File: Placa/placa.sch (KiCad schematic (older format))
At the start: 23 parts

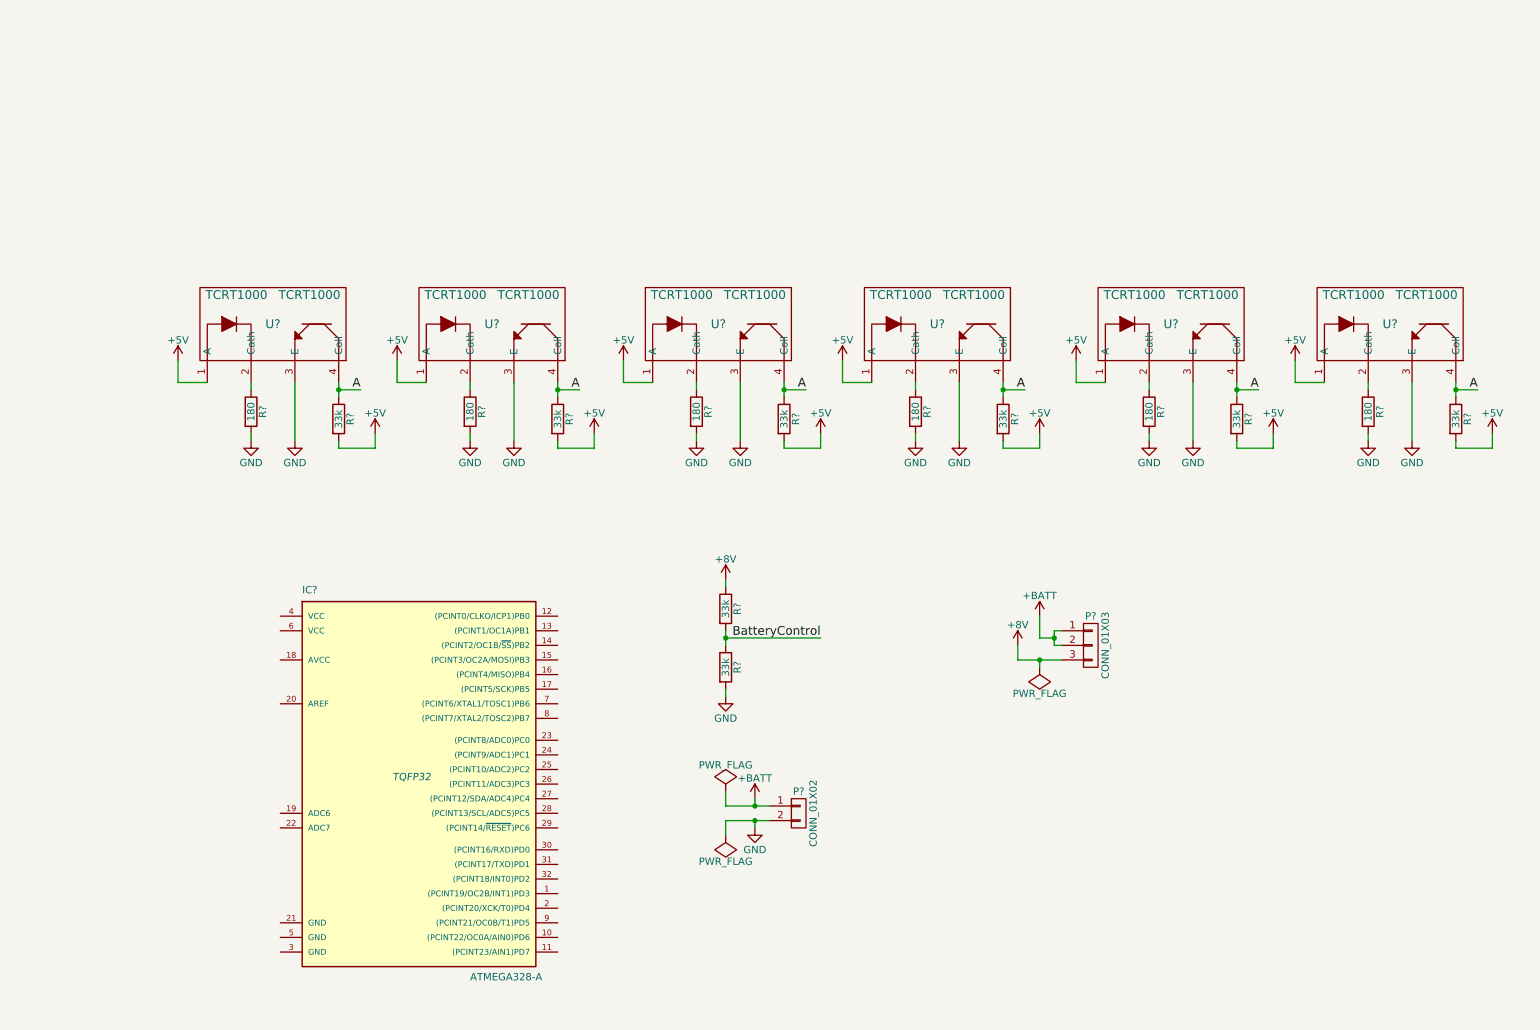
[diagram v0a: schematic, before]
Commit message: Agregados reguladores de tension en el PCB. Falta el puente H
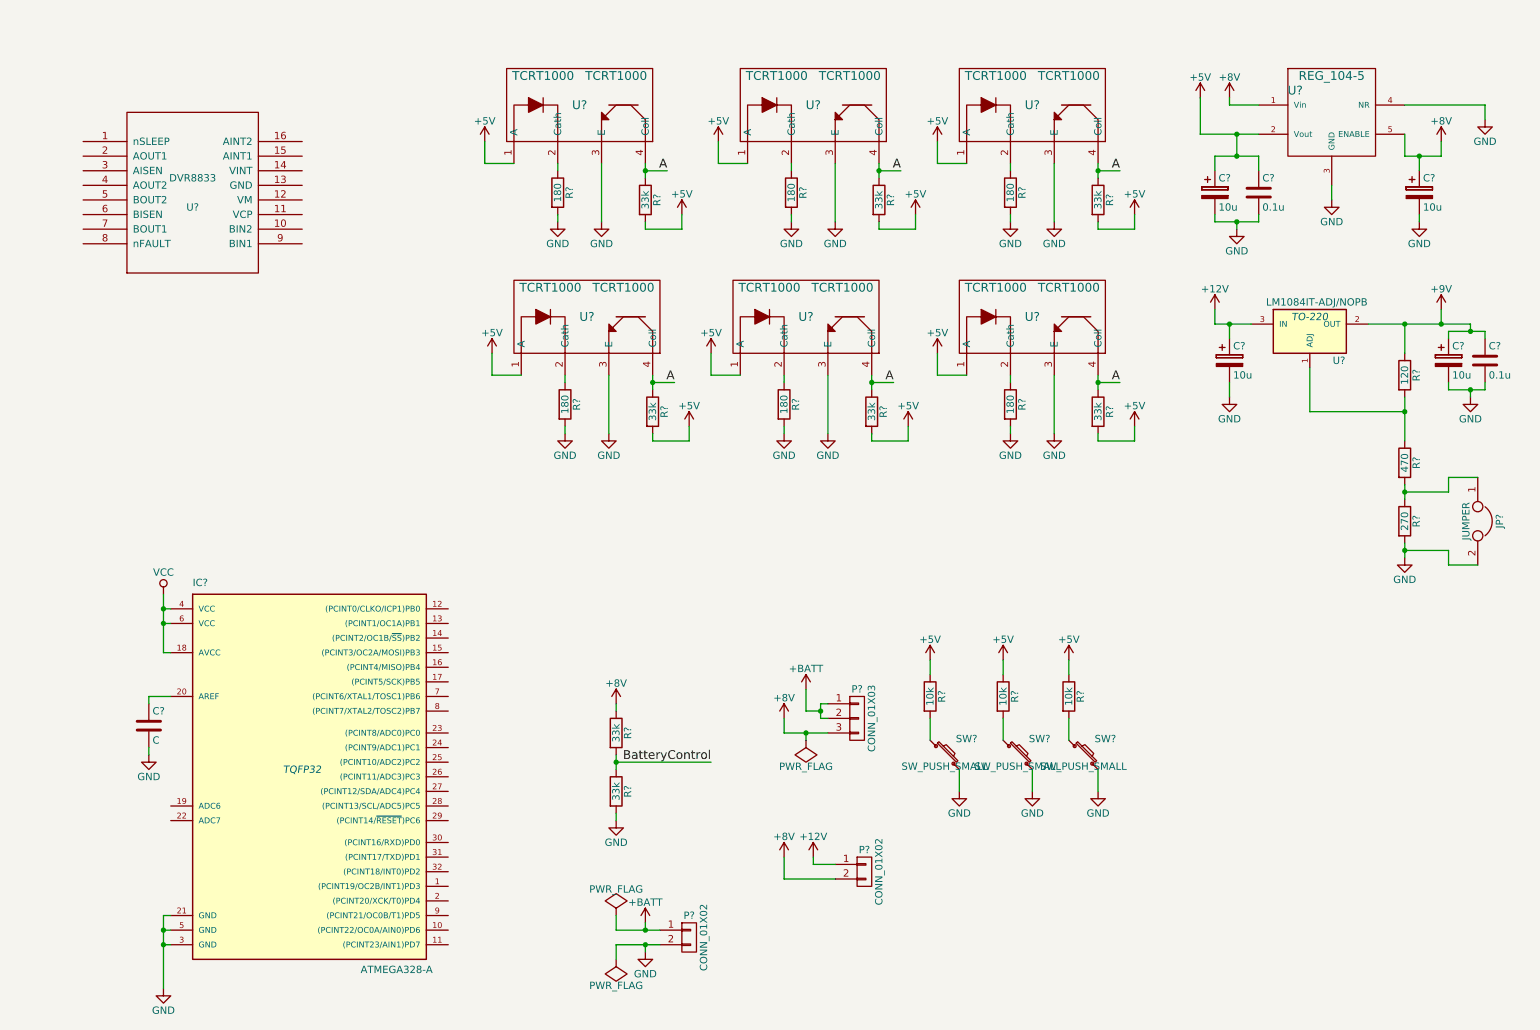
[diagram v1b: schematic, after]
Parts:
- added C? (x4): 10u, symbol CP
- added C? (x2): 0.1u, symbol C
- added C?: C, symbol C
- added JP?: JUMPER, symbol JUMPER
- added P?: CONN_01X02, symbol CONN_01X02
- added R? (x3): 10k, symbol R
- added R?: 120, symbol R
- added R?: 470, symbol R
- added R?: 270, symbol R
- added SW? (x3): SW_PUSH_SMALL, symbol SW_PUSH_SMALL
- added U?: REG_104-5, symbol REG_104-5
- added U?: LM1084IT-ADJ/NOPB, TO-220, symbol LM1084IT-ADJ/NOPB
- added U?: DVR8833, MODULE, symbol DVR8833
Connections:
- net +5V: now also C?.1, C?.1, R?.1, R?.1, R?.1, U?.2 (Vout)
- net +8V: now also C?.1, P?.2 (P2), U?.1 (Vin), U?.5 (ENABLE)
- net GND: now also IC?.21 (GND), IC?.3 (GND), IC?.5 (GND), C?.2, C?.2, C?.2, C?.2, C?.2, C?.2, C?.2, JP?.2, R?.2, SW?.2, SW?.2, SW?.2, U?.3 (GND), U?.4 (NR)
- net VCC: now reaches IC?.18 (AVCC)
- net VCC: now also IC?.4 (VCC), IC?.6 (VCC)
- net at IC?.20 (AREF): now also C?.1
- new net: R?.2, SW?.1 (x3)
- new net: R?.1, R?.2, U?.1 (ADJ)
- new net: JP?.1, R?.1, R?.2
- new net +12V: C?.1, P?.1 (P1), U?.3 (IN)
- new net +9V: C?.1, C?.1, R?.1, U?.2 (OUT)
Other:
- moved on the sheet: IC?, P?, R?, U?

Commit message: Agregados sub-esquemáticos. Avances en la placa.
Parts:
- removed R? (x6): 180, symbol R
- removed R? (x6): 33k, symbol R
- removed U? (x6): TCRT1000, TCRT1000, symbol TCRT1000
- removed U?: DVR8833, MODULE, symbol DVR8833
- added P?: CONN_01X03, symbol CONN_01X03
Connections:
- net labels added: Boton1, Boton2, Boton3, M1IN1, M1IN2, M1OUT1, M1OUT2, M1VCP, M1VINT, M2IN1, M2IN2, M2OUT1, M2OUT2, M2VCP, M2VINT, Sensor1, Sensor2, Sensor3, Sensor4, Sensor5, Sensor6, VDD, VPP
- net labels removed: A, VCC
- wire segments 148 -> 132
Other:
- moved on the sheet: P?, R?, SW?

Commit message: Avances sobre la placa.
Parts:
- removed C? (x4): 10u, symbol CP
- removed C? (x2): 0.1u, symbol C
- removed JP?: JUMPER, symbol JUMPER
- removed P? (x2): CONN_01X03, symbol CONN_01X03
- removed P? (x2): CONN_01X02, symbol CONN_01X02
- removed R?: 120, symbol R
- removed R?: 470, symbol R
- removed R?: 270, symbol R
- removed U?: REG_104-5, symbol REG_104-5
- removed U?: LM1084IT-ADJ/NOPB, TO-220, symbol LM1084IT-ADJ/NOPB
- added D2, D3, D4, D5: LED, LEDs:LED_0805, symbol LED
- added P1: CONN_01X04, Pin_Headers:Pin_Header_Straight_1x04, symbol CONN_01X04
- added P2, P3: CONN_01X02, Pin_Headers:Pin_Header_Straight_1x02, symbol CONN_01X02
- added R2: 10k, Resistors_SMD:R_0805, symbol R
- added R25, R26, R27, R28: 220, Resistors_SMD:R_0805, symbol R
- added SW1: SW_PUSH_SMALL, Buttons_Switches_ThroughHole:SW_PUSH_SMALL, symbol SW_PUSH_SMALL
- C1: renamed from C?; footprint (none) -> Capacitors_ThroughHole:C_Radial_D5_L11_P2
- IC1: renamed from IC?; footprint TQFP32 -> Housings_QFP:TQFP-32_7x7mm_Pitch0.8mm
- R3, R4, R5, R6, R7: renamed from R?; footprint (none) -> Resistors_SMD:R_0805
- SW2, SW3, SW4: renamed from SW?; footprint (none) -> Buttons_Switches_ThroughHole:SW_PUSH_SMALL
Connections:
- net labels added: Habilitador1, Habilitador2, Led1, Led2, Led3, Led4, RX, Reset, TX
- net labels removed: +12V, +9V, M1VCP, M2VCP, VDD
- wire segments 132 -> 106
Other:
- moved on the sheet: R4, R5

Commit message: Más avances en placa. Ignorados archivos bak.
Falta corregir algunas cosas en el esquemático, relacionado con los motores. El pcb está apenas empezado.
Se ignoraron los archivos bak y cache de kicad.
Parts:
- added P12: CONN_02X03, Pin_Headers:Pin_Header_Straight_2x03, symbol CONN_02X03
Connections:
- net labels added: Miso, Mosi, Sck
- wire segments 106 -> 114
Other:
- note added: "Conector Serie"
- note added: "Conector programador ISP\n"
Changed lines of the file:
@@
 LIBS:reg_204-5
 LIBS:DVR8833
-LIBS:placa-cache
 EELAYER 25 0
 EELAYER END
@@
 	10350 5350 10700 5350
 Connection ~ 10700 5350
-Text Label 4100 4950 2    60   ~ 0
+Text Label 4100 4450 2    60   ~ 0
 Boton1
 Text Label 4100 5050 2    60   ~ 0
@@
 F4 "M2VINT" I L 3600 2000 60
 F5 "VM" I L 3600 1050 60
-F7 "M2OUT1" I L 3600 1450 60
-F8 "M2OUT2" I L 3600 1600 60
-F9 "M1IN2" I R 5100 2450 60
-F10 "M1IN1" I R 5100 2250 60
-F11 "M1VINT" I R 5100 2000 60
-F13 "M1OUT1" I R 5100 1450 60
-F14 "M1OUT2" I R 5100 1600 60
+F6 "M2OUT1" I L 3600 1450 60
+F7 "M2OUT2" I L 3600 1600 60
+F8 "M1IN2" I R 5100 2450 60
+F9 "M1IN1" I R 5100 2250 60
+F10 "M1VINT" I R 5100 2000 60
+F11 "M1OUT1" I R 5100 1450 60
+F12 "M1OUT2" I R 5100 1600 60
 $EndSheet
 $Sheet
@@
 Text Label 8200 1900 2    60   ~ 0
 Habilitador2
-Text Label 4300 4850 2    60   ~ 0
+Text Label 4350 6750 2    60   ~ 0
 Habilitador2
-Text Label 4300 4750 2    60   ~ 0
+Text Label 4300 6450 2    60   ~ 0
 Habilitador1
 Wire Wire Line
-	4300 4850 3750 4850
-Wire Wire Line
-	3750 4750 4300 4750
+	3750 4850 4700 4850
+Wire Wire Line
+	3750 4750 4700 4750
 Text Label 8550 4200 0    60   ~ 0
 M2OUT1
 Text Label 8550 4300 0    60   ~ 0
 M2OUT2
-Text Label 4100 6350 2    60   ~ 0
-M2VINT
 Text Label 4050 4550 2    60   ~ 0
 M2IN1
@@
 Text Label 8550 3700 0    60   ~ 0
 M1OUT2
-Text Label 4100 6250 2    60   ~ 0
-M1VINT
 Text Label 4050 6650 2    60   ~ 0
 M1IN1
@@
 	4050 4650 3750 4650
 Wire Wire Line
-	4100 4950 3750 4950
+	3750 4950 4650 4950
 Wire Wire Line
 	4100 5050 3750 5050
@@
 L CONN_01X04 P1
 U 1 1 572D968E
-P 8250 5400
-F 0 "P1" H 8250 5650 50  0000 C CNN
-F 1 "CONN_01X04" V 8350 5400 50  0000 C CNN
-F 2 "Pin_Headers:Pin_Header_Straight_1x04" H 8250 5400 50  0001 C CNN
-F 3 "" H 8250 5400 50  0000 C CNN
-	1    8250 5400
-	1    0    0    -1
-$EndComp
-Wire Wire Line
-	8050 5250 7900 5250
-Wire Wire Line
-	7900 5250 7900 5150
+P 8250 5350
+F 0 "P1" H 8250 5600 50  0000 C CNN
+F 1 "CONN_01X04" V 8350 5350 50  0000 C CNN
+F 2 "Pin_Headers:Pin_Header_Straight_1x04" H 8250 5350 50  0001 C CNN
+F 3 "" H 8250 5350 50  0000 C CNN
+	1    8250 5350
+	1    0    0    -1
+$EndComp
+Wire Wire Line
+	8050 5200 7900 5200
+Wire Wire Line
+	7900 5200 7900 5100
 $Comp
 L +5V #PWR017
 U 1 1 572DB105
-P 7900 5150
-F 0 "#PWR017" H 7900 5000 50  0001 C CNN
-F 1 "+5V" H 7900 5290 50  0000 C CNN
-F 2 "" H 7900 5150 50  0000 C CNN
-F 3 "" H 7900 5150 50  0000 C CNN
-	1    7900 5150
-	1    0    0    -1
-$EndComp
-Wire Wire Line
-	8050 5550 7900 5550
-Text Label 7900 5350 0    60   ~ 0
+P 7900 5100
+F 0 "#PWR017" H 7900 4950 50  0001 C CNN
+F 1 "+5V" H 7900 5240 50  0000 C CNN
+F 2 "" H 7900 5100 50  0000 C CNN
+F 3 "" H 7900 5100 50  0000 C CNN
+	1    7900 5100
+	1    0    0    -1
+$EndComp
+Wire Wire Line
+	8050 5500 7900 5500
+Text Label 7900 5300 0    60   ~ 0
 TX
 Wire Wire Line
-	7600 5450 8050 5450
-Wire Wire Line
-	7900 5350 8050 5350
-Wire Wire Line
-	7600 5450 7600 5550
+	7600 5400 8050 5400
+Wire Wire Line
+	7900 5300 8050 5300
+Wire Wire Line
+	7600 5400 7600 5500
 $Comp
 L GND #PWR018
 U 1 1 572DBC53
-P 7600 5550
-F 0 "#PWR018" H 7600 5300 50  0001 C CNN
-F 1 "GND" H 7600 5400 50  0000 C CNN
-F 2 "" H 7600 5550 50  0000 C CNN
-F 3 "" H 7600 5550 50  0000 C CNN
-	1    7600 5550
-	1    0    0    -1
-$EndComp
-Text Label 7900 5550 0    60   ~ 0
+P 7600 5500
+F 0 "#PWR018" H 7600 5250 50  0001 C CNN
+F 1 "GND" H 7600 5350 50  0000 C CNN
+F 2 "" H 7600 5500 50  0000 C CNN
+F 3 "" H 7600 5500 50  0000 C CNN
+	1    7600 5500
+	1    0    0    -1
+$EndComp
+Text Label 7900 5500 0    60   ~ 0
 RX
 Text Label 3900 6150 2    60   ~ 0
@@
 Text Label 1800 3550 0    60   ~ 0
 Led2
-Text Label 4000 6450 2    60   ~ 0
+Text Label 4000 4750 2    60   ~ 0
 Led1
 Wire Wire Line
-	3750 4450 4000 4450
-Text Label 4000 6750 2    60   ~ 0
-Led2
-Wire Wire Line
-	3750 6450 4000 6450
-Text Label 4000 4450 2    60   ~ 0
+	3750 4450 4100 4450
+Wire Wire Line
+	3750 6450 4300 6450
+Text Label 4000 4950 2    60   ~ 0
 Led3
 Wire Wire Line
-	4000 6750 3750 6750
+	4350 6750 3750 6750
 Text Label 4000 5800 2    60   ~ 0
 Led4
@@
 Wire Wire Line
 	4000 5800 3750 5800
+$Comp
+L CONN_02X03 P12
+U 1 1 57365B2B
+P 6900 3850
+F 0 "P12" H 6900 4050 50  0000 C CNN
+F 1 "CONN_02X03" H 6900 3650 50  0000 C CNN
+F 2 "Pin_Headers:Pin_Header_Straight_2x03" H 6900 2650 50  0001 C CNN
+F 3 "" H 6900 2650 50  0000 C CNN
+	1    6900 3850
+	1    0    0    -1
+$EndComp
+Text Label 6400 3750 0    60   ~ 0
+Miso
+Wire Wire Line
+	6400 3750 6650 3750
+Wire Wire Line
+	7150 3750 7400 3750
+Wire Wire Line
+	7400 3750 7400 3600
+$Comp
+L +5V #PWR025
+U 1 1 573660BC
+P 7400 3600
+F 0 "#PWR025" H 7400 3450 50  0001 C CNN
+F 1 "+5V" H 7400 3740 50  0000 C CNN
+F 2 "" H 7400 3600 50  0000 C CNN
+F 3 "" H 7400 3600 50  0000 C CNN
+	1    7400 3600
+	1    0    0    -1
+$EndComp
+Wire Wire Line
+	7150 3950 7400 3950
+Wire Wire Line
+	7400 3950 7400 4100
+$Comp
+L GND #PWR026
+U 1 1 57366261
+P 7400 4100
+F 0 "#PWR026" H 7400 3850 50  0001 C CNN
+F 1 "GND" H 7400 3950 50  0000 C CNN
+F 2 "" H 7400 4100 50  0000 C CNN
+F 3 "" H 7400 4100 50  0000 C CNN
+	1    7400 4100
+	1    0    0    -1
+$EndComp
+Text Label 7400 3850 2    60   ~ 0
+Mosi
+Wire Wire Line
+	7400 3850 7150 3850
+Text Label 6450 3850 0    60   ~ 0
+Sck
+Wire Wire Line
+	6450 3850 6650 3850
+Text Label 6350 3950 0    60   ~ 0
+Reset
+Wire Wire Line
+	6350 3950 6650 3950
+Text Label 4700 4850 2    60   ~ 0
+Miso
+Text Label 4650 4950 2    60   ~ 0
+Sck
+Text Label 4700 4750 2    60   ~ 0
+Mosi
+Text Notes 6400 3350 0    60   ~ 0
+Conector programador ISP\n
+Text Label 4000 4850 2    60   ~ 0
+Led2
+Text Notes 7600 4850 0    60   ~ 0
+Conector Serie
+Wire Notes Line
+	7400 4700 7400 5750
+Wire Notes Line
+	7400 5750 8500 5750
+Wire Notes Line
+	8500 5750 8500 4700
+Wire Notes Line
+	8500 4700 7400 4700
+Wire Notes Line
+	6250 3150 6250 4350
+Wire Notes Line
+	6250 4350 7650 4350
+Wire Notes Line
+	7650 4350 7650 3150
+Wire Notes Line
+	7650 3150 6250 3150
 $EndSCHEMATC

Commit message: Cambio prematuro de etiquetas para saber qué cosas hay que cambiar.
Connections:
- net labels added: BotonExtra, EncoderM1, EncoderM2, M1IN1(PWM), M2IN1(PWM), Sensor7, XTAL1, XTAL2
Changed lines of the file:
@@
 Text Label 4100 4450 2    60   ~ 0
 Boton1
-Text Label 4100 5050 2    60   ~ 0
+Text Label 4350 6750 2    60   ~ 0
 Boton2
-Text Label 4100 5150 2    60   ~ 0
-Boton3
+Text Label 4500 6150 2    60   ~ 0
+BotonExtra
 Text Label 1200 5800 0    60   ~ 0
 BatteryControl
@@
 Text Label 8200 1900 2    60   ~ 0
 Habilitador2
-Text Label 4350 6750 2    60   ~ 0
+Text Label 5550 6100 2    60   ~ 0
 Habilitador2
 Text Label 4300 6450 2    60   ~ 0
@@
 Text Label 8550 4300 0    60   ~ 0
 M2OUT2
-Text Label 4050 4550 2    60   ~ 0
-M2IN1
-Text Label 4050 4650 2    60   ~ 0
+Text Label 4300 4550 2    60   ~ 0
+M2IN1(PWM)
+Text Label 4050 6650 2    60   ~ 0
 M2IN2
 Text Label 8550 3600 0    60   ~ 0
@@
 Text Label 8550 3700 0    60   ~ 0
 M1OUT2
-Text Label 4050 6650 2    60   ~ 0
-M1IN1
+Text Label 4300 4650 2    60   ~ 0
+M1IN1(PWM)
 Text Label 4050 6550 2    60   ~ 0
 M1IN2
@@
 	4100 5150 3750 5150
 Wire Wire Line
-	4100 6250 3750 6250
-Wire Wire Line
-	4100 6350 3750 6350
+	3750 6250 4500 6250
+Wire Wire Line
+	3750 6350 4500 6350
 $Comp
 L CONN_01X04 P1
@@
 TX
 Wire Wire Line
-	3900 6150 3750 6150
+	3750 6150 4500 6150
 Text Label 3900 6050 2    60   ~ 0
 RX
 Wire Wire Line
-	3900 6050 3750 6050
+	3750 6050 4500 6050
 $Comp
 L +5V #PWR17
@@
 Wire Wire Line
 	4350 6750 3750 6750
-Text Label 4000 5800 2    60   ~ 0
+Text Label 5650 6300 2    60   ~ 0
 Led4
 Wire Wire Line
 	1500 5900 1850 5900
 Wire Wire Line
-	4000 5800 3750 5800
+	3750 5800 4150 5800
 $Comp
 L CONN_02X03 P12
@@
 Wire Notes Line
 	7650 3150 6250 3150
+Text Label 4100 5050 2    60   ~ 0
+XTAL1
+Text Label 4100 5150 2    60   ~ 0
+XTAL2
+Text Label 4500 6350 2    60   ~ 0
+EncoderM2
+Text Label 4500 6250 2    60   ~ 0
+EncoderM1
+Text Label 4150 5800 2    60   ~ 0
+Sensor7
 $EndSCHEMATC

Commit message: Modificaciones a la placa
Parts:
- removed D5: LED, LEDs:LED_0805, symbol LED
- removed R28: 220, Resistors_SMD:R_0805, symbol R
- added Cristal1: Crystal, symbol Crystal
- added Cxtal1, Cxtal2: 22p, symbol C
- added P4: BallCaster2, symbol CONN_01X02
- added P5: BallCaster1, symbol CONN_01X02
- added P6, P7: CONN_01X04, symbol CONN_01X04
- added U11: sn74lvc2g86, symbol sn74lvc2g86
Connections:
- net labels added: Habilitador
- net labels removed: +8V, Boton3, Habilitador1, Habilitador2, Led4, M1IN1(PWM), M2IN1(PWM)
- wire segments 114 -> 148
- no-connect marks 0 -> 4

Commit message: se termino el esquematico y asociacion de componentes, falta acomodar y rutear PCB
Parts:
- Cristal1: footprint (none) -> Crystals:Crystal_HC50-U_Vertical
- Cxtal1, Cxtal2: footprint (none) -> Capacitors_SMD:C_0805_HandSoldering
- P4, P5: footprint (none) -> ballcaster:Pin_Header_Straight_1x02
- P6, P7: footprint (none) -> Pin_Headers:Pin_Header_Straight_1x04
- SW1, SW4: footprint Buttons_Switches_ThroughHole:SW_PUSH_SMALL -> Buttons_Switches_SMD:SW_SPST_B3U-1000P
- U11: footprint (none) -> Housings_SSOP:TSSOP-8_3x3mm_Pitch0.65mm
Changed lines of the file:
@@
 F 0 "SW4" H 10950 5660 50  0000 C CNN
 F 1 "SW_PUSH_SMALL" H 10800 5471 50  0000 C CNN
-F 2 "Buttons_Switches_ThroughHole:SW_PUSH_SMALL" H 10800 5550 50  0001 C CNN
+F 2 "Buttons_Switches_SMD:SW_SPST_B3U-1000P" H 10800 5550 50  0001 C CNN
 F 3 "" H 10800 5550 50  0000 C CNN
 	1    10800 5550
@@
 F 0 "SW1" H 9200 5660 50  0000 C CNN
 F 1 "SW_PUSH_SMALL" H 9050 5471 50  0000 C CNN
-F 2 "Buttons_Switches_ThroughHole:SW_PUSH_SMALL" H 9050 5550 50  0001 C CNN
+F 2 "Buttons_Switches_SMD:SW_SPST_B3U-1000P" H 9050 5550 50  0001 C CNN
 F 3 "" H 9050 5550 50  0000 C CNN
 	1    9050 5550
@@
 F 0 "Cristal1" H 5900 5300 50  0000 C CNN
 F 1 "Crystal" H 5900 5000 50  0000 C CNN
-F 2 "" H 5900 5150 50  0000 C CNN
+F 2 "Crystals:Crystal_HC50-U_Vertical" H 5900 5150 50  0001 C CNN
 F 3 "" H 5900 5150 50  0000 C CNN
 	1    5900 5150
@@
 F 0 "Cxtal1" H 6825 5350 50  0000 L CNN
 F 1 "22p" H 6825 5150 50  0000 L CNN
-F 2 "" H 6838 5100 50  0000 C CNN
+F 2 "Capacitors_SMD:C_0805_HandSoldering" H 6838 5100 50  0001 C CNN
 F 3 "" H 6800 5250 50  0000 C CNN
 	1    6800 5250
@@
 F 0 "Cxtal2" H 6425 5350 50  0000 L CNN
 F 1 "22p" H 6425 5150 50  0000 L CNN
-F 2 "" H 6438 5100 50  0000 C CNN
+F 2 "Capacitors_SMD:C_0805_HandSoldering" H 6438 5100 50  0001 C CNN
 F 3 "" H 6400 5250 50  0000 C CNN
 	1    6400 5250
@@
 F 0 "U11" H 10200 1350 50  0000 C CNN
 F 1 "sn74lvc2g86" H 10200 1250 50  0000 C CNN
-F 2 "" H 10200 1300 50  0000 C CNN
+F 2 "Housings_SSOP:TSSOP-8_3x3mm_Pitch0.65mm" H 10200 1300 50  0001 C CNN
 F 3 "" H 10200 1300 50  0000 C CNN
 	1    10200 1300
@@
 F 0 "U11" H 10200 2200 50  0000 C CNN
 F 1 "sn74lvc2g86" H 10200 2100 50  0000 C CNN
-F 2 "" H 10200 2150 50  0000 C CNN
+F 2 "Housings_SSOP:TSSOP-8_3x3mm_Pitch0.65mm" H 10200 2150 50  0001 C CNN
 F 3 "" H 10200 2150 50  0000 C CNN
 	2    10200 2150
@@
 F 0 "P6" H 9000 1550 50  0000 C CNN
 F 1 "CONN_01X04" V 9100 1300 50  0000 C CNN
-F 2 "" H 9000 1300 50  0000 C CNN
+F 2 "Pin_Headers:Pin_Header_Straight_1x04" H 9000 1300 50  0001 C CNN
 F 3 "" H 9000 1300 50  0000 C CNN
 	1    9000 1300
@@
 F 0 "P7" H 9000 2400 50  0000 C CNN
 F 1 "CONN_01X04" V 9100 2150 50  0000 C CNN
-F 2 "" H 9000 2150 50  0000 C CNN
+F 2 "Pin_Headers:Pin_Header_Straight_1x04" H 9000 2150 50  0001 C CNN
 F 3 "" H 9000 2150 50  0000 C CNN
 	1    9000 2150
@@
 F 0 "P4" H 6000 6400 50  0000 C CNN
 F 1 "BallCaster2" V 6100 6250 50  0000 C CNN
-F 2 "" H 6000 6250 50  0000 C CNN
+F 2 "ballcaster:Pin_Header_Straight_1x02" H 6000 6250 50  0001 C CNN
 F 3 "" H 6000 6250 50  0000 C CNN
 	1    6000 6250
@@
 F 0 "P5" H 6000 6950 50  0000 C CNN
 F 1 "BallCaster1" V 6100 6800 50  0000 C CNN
-F 2 "" H 6000 6800 50  0000 C CNN
+F 2 "ballcaster:Pin_Header_Straight_1x02" H 6000 6800 50  0001 C CNN
 F 3 "" H 6000 6800 50  0000 C CNN
 	1    6000 6800
